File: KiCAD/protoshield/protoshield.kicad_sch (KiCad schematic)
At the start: 34 parts, among them J1 Screw_Terminal_01x03, J16 Screw_Terminal_01x05, J2 Screw_Terminal_01x02, J3 Screw_Terminal_01x02, J4 Screw_Terminal_01x02, J5 Screw_Terminal_01x02, J6 Screw_Terminal_01x03, J7 Screw_Terminal_01x03, J8 Screw_Terminal_01x03, U2 Metro_ESP32S3

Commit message: revD: Metro symbol gains SDA/SCL + protoshield wiring + analog update
xmitter.kicad_sym Metro_ESP32S3 symbol: add SDA and SCL pins
(bidirectional) at (15.24, +16.51) and (15.24, +19.05); expand body
top from +17.145 to +21.59; move Reference label to +22.86. No other
pins moved.

Protoshield schematic: wire the new Metro SDA/SCL pins through the
shield's screw-terminal boundary to the analog board I2C LV-side
entry.

Analog arduino.kicad_sch: companion updates picked up during the
I2C routing work.

Co-Authored-By: Claude Opus 4.7 <noreply@anthropic.com>
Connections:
- net SCL_IN: now also U2.SCL
- net SDA_IN: now also U2.SDA
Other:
- note added: "SCL_IN and SDA_IN go to SCL and SDA"
- note removed: "SCL_IN and SDA_IN go to SCL and SDA on Metro (not shown in symbol)"
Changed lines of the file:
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@@
 	(generator_version "10.0")
 	(paper "A4")
-	(text "SCL_IN and SDA_IN go to SCL and SDA\non Metro (not shown in symbol)"
+	(text "SCL_IN and SDA_IN go to SCL and SDA"
 		(exclude_from_sim no)
 		(at 118.618 143.764 0)
@@
 	)
 	(global_label "SCL_IN"
-		(shape output)
+		(shape bidirectional)
 		(at 107.95 142.24 0)
 		(fields_autoplaced yes)
@@
 		)
 		(property "Intersheetrefs" "${INTERSHEET_REFS}"
-			(at 117.3457 142.24 0)
+			(at 118.457 142.24 0)
 			(hide yes)
 			(show_name no)
@@
 		)
 	)
+	(global_label "SCL_IN"
+		(shape bidirectional)
+		(at 181.61 64.77 0)
+		(fields_autoplaced yes)
+		(effects
+			(font
+				(size 1.27 1.27)
+			)
+			(justify left)
+		)
+		(property "Intersheetrefs" "${INTERSHEET_REFS}"
+			(at 192.117 64.77 0)
+			(hide yes)
+			(show_name no)
+			(do_not_autoplace no)
+			(effects
+				(font
+					(size 1.27 1.27)
+				)
+				(justify left)
+			)
+		)
+	)
 	(global_label "FAULT_N_CLEAN"
 		(shape input)
@@
 	)
 	(global_label "SDA_IN"
-		(shape output)
+		(shape bidirectional)
 		(at 107.95 144.78 0)
 		(fields_autoplaced yes)
@@
 		)
 		(property "Intersheetrefs" "${INTERSHEET_REFS}"
-			(at 117.4062 144.78 0)
+			(at 118.5175 144.78 0)
 			(hide yes)
 			(show_name no)
@@
 		)
 	)
+	(global_label "SDA_IN"
+		(shape bidirectional)
+		(at 181.61 67.31 0)
+		(fields_autoplaced yes)
+		(effects
+			(font
+				(size 1.27 1.27)
+			)
+			(justify left)
+		)
+		(property "Intersheetrefs" "${INTERSHEET_REFS}"
+			(at 192.1775 67.31 0)
+			(hide yes)
+			(show_name no)
+			(do_not_autoplace no)
+			(effects
+				(font
+					(size 1.27 1.27)
+				)
+				(justify left)
+			)
+		)
+	)
 	(global_label "Source_Sense_B"
 		(shape input)
@@
 		(pin "RESET"
 		)
+		(pin "SCL"
+		)
+		(pin "SDA"
+		)
 		(instances

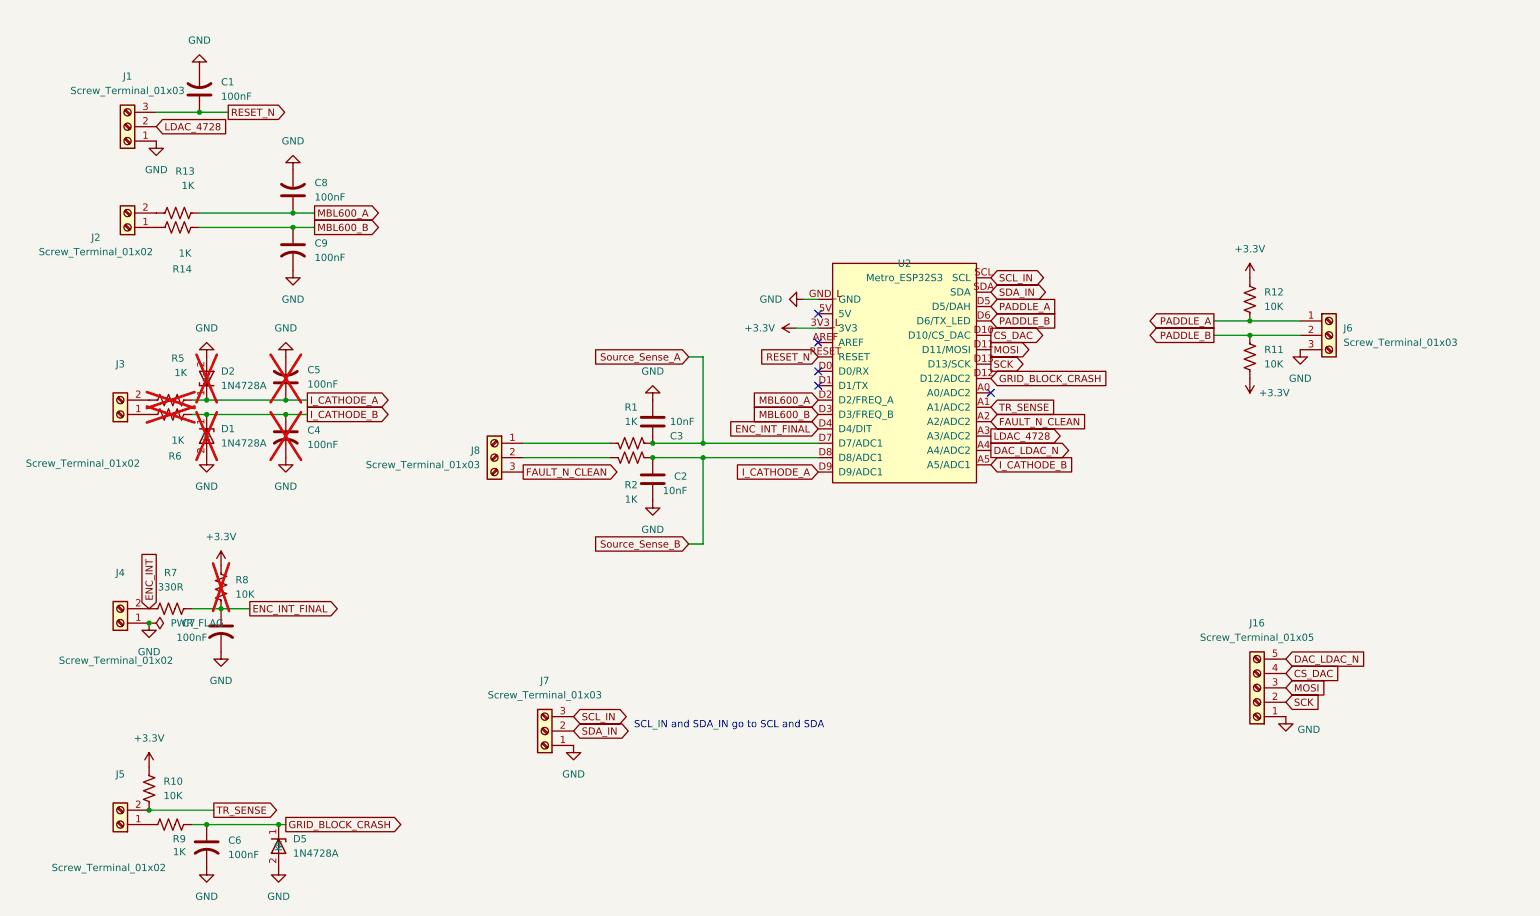
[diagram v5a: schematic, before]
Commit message: revD: Documentation handoff snapshot + protoshield/analog touch-ups
New Documentation/revD_fix_status_2026-10-24.md: handoff doc capturing
the 2026-10-22 to 10-24 claude.ai review session state -- decisions
made, schematic changes landed, items still open, with cross-refs to
the Rev D Fix Implementation Plan item IDs (A1, P2, F3, ... M/S/N).

Documentation/Components/cd54hc4049.pdf: TI CD54/74HC4049 and HC4050
datasheet archived locally.

Analog + protoshield minor schematic touches picked up during
reconciliation; netlists regenerated to match.

Co-Authored-By: Claude Opus 4.7 <noreply@anthropic.com>
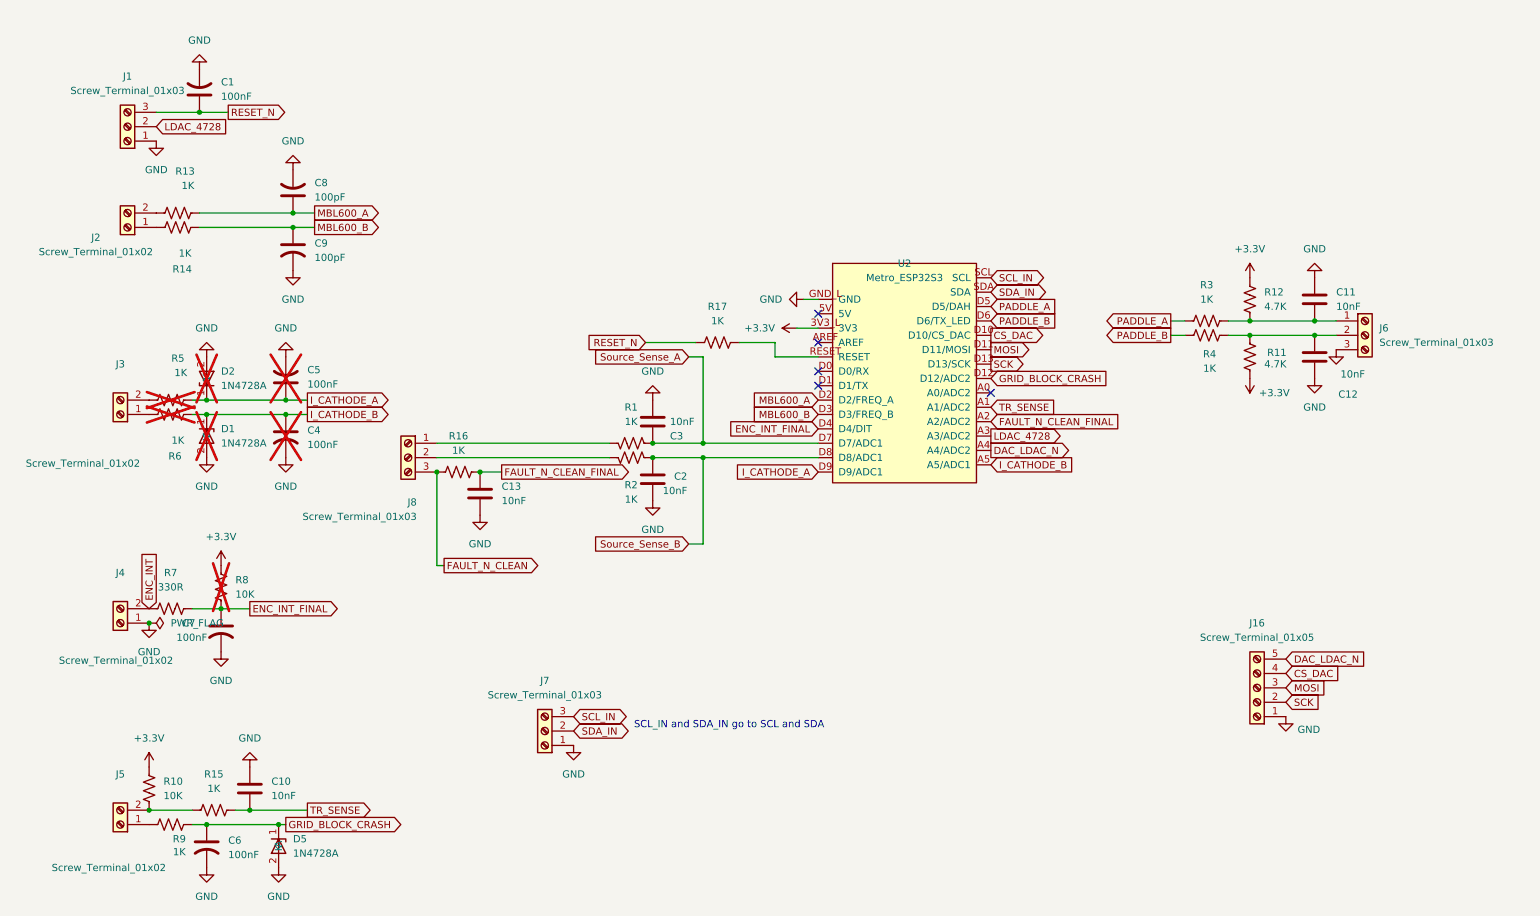
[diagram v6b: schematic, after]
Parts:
- added C10, C11, C12, C13: 10nF, symbol Device:C
- added R15, R16, R17, R3, R4: 1K, symbol Device:R_US
- C8, C9: value 100nF -> 100pF
- R11, R12: value 10K -> 4.7K
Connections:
- net FAULT_N_CLEAN: now also R16.1; no longer U2.A2 (A2/ADC2)
- net GND: now also C10.1, C11.1, C12.1, C13.2
- net PADDLE_A: now also R3.1; no longer J6.1 (Pin_1), R12.2
- net PADDLE_B: now also R4.1; no longer J6.2 (Pin_2), R11.1
- net RESET_N: now also R17.1; no longer U2.RESET
- net TR_SENSE: now also C10.2, R15.2; no longer J5.2 (Pin_2), R10.2
- new net: C11.2, J6.1 (Pin_1), R12.2, R3.2
- new net: C12.2, J6.2 (Pin_2), R11.1, R4.2
- new net: J5.2 (Pin_2), R10.2, R15.1
- new net: R17.2, U2.RESET
- new net FAULT_N_CLEAN_FINAL: C13.1, R16.2, U2.A2 (A2/ADC2)
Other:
- moved on the sheet: J6, J8

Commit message: revD: footprint pass across all boards + ss_pa fault-chain fix + LLM review brief
- New tools/assign_misc_footprints.py: lib_id-keyed footprint assigner
  (resistors, screw terminals, pin headers, LT1054); mirrors cap-script
  safe-write (UTF-8 no BOM, no CRLF translation).
- tools/assign_cap_footprints.py: added 0.47uF -> C_Rect_L7.0mm case.
- Ran both scripts across analog, ss_pa, Output LPF, frontpanel,
  protoshield, and shelved power board. ~100 fills; details in diffs.
- ss_pa: R1-R4 (0.22 ohm source sense) upgraded to 2W Yageo RSF200
  with DIN0516 L15.5mm/P20.32mm footprint; Value tagged "0.22R 2W".
  R15/R16 confirmed 1/4W (DIN0207) for BS170 source degeneration.
- analog/power: R44 15R 5W horizontal, P30.48mm footprint.
- ss_pa fault chain (from external LLM review): R21/R22 raised
  10K -> 100K to restore self-latching loop gain; new R26 = 100K
  across C12 so cap discharges between power cycles (reliable reset).
  R26 footprint pending.
- Documentation/revD_llm_review_brief.md: new, comprehensive system
  description for external LLM deep-dive (function, component values,
  power dissipation, design flaws). References all five board netlists.

Co-Authored-By: Claude Opus 4.7 <noreply@anthropic.com>
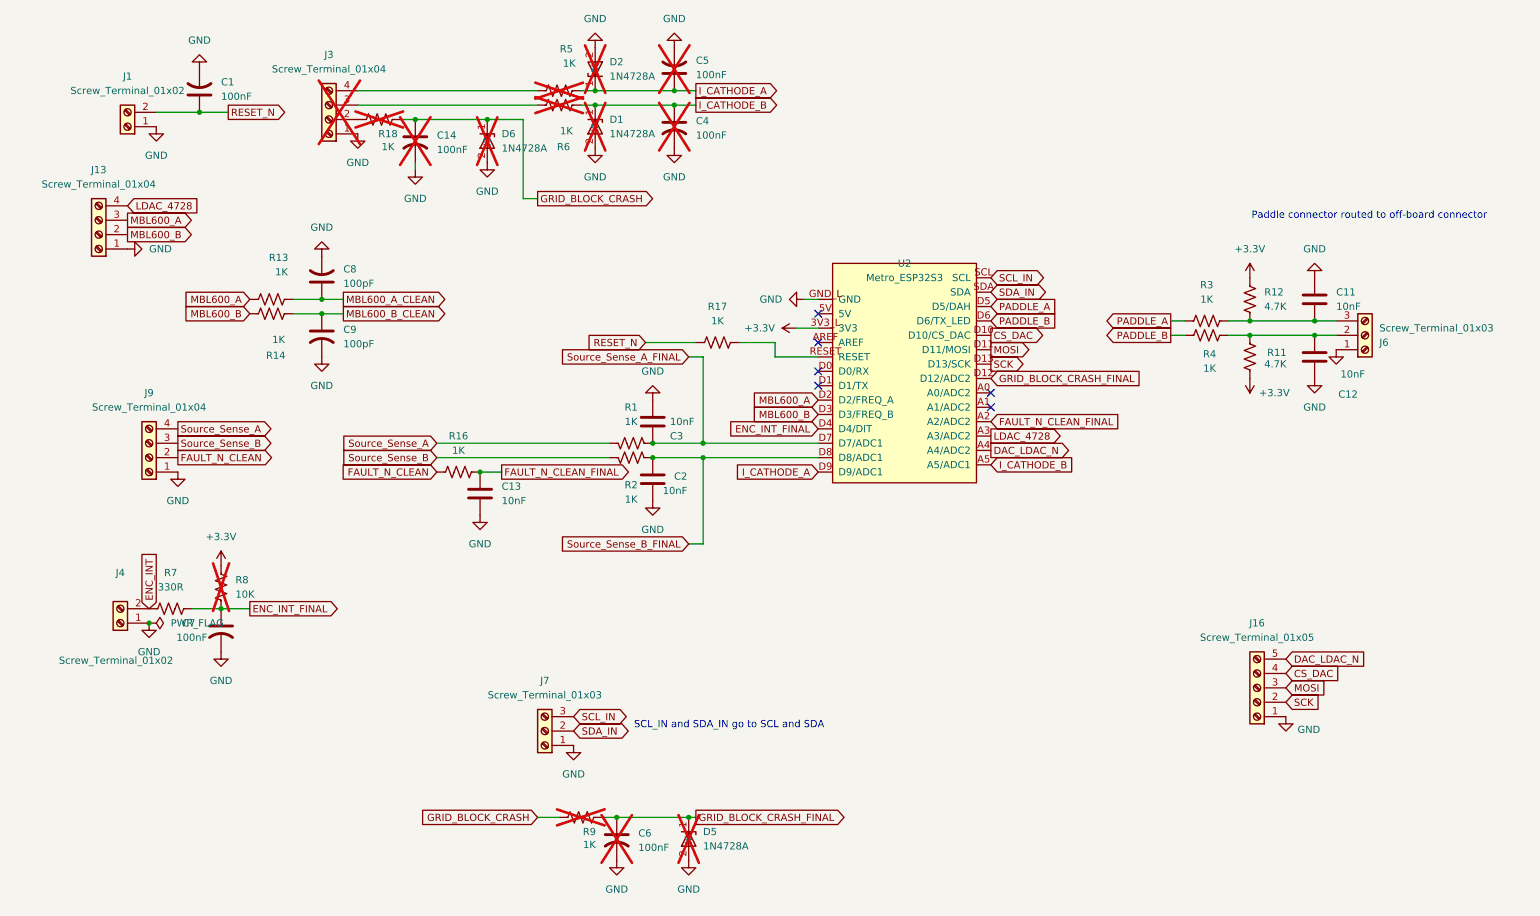
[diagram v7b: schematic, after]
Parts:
- removed C10: 10nF, symbol Device:C
- removed J1, J8: Screw_Terminal_01x03, TerminalBlock_Phoenix:TerminalBlock_Phoenix_MKDS-1,5-3_1x03_P5.00mm_Horizontal, symbol Connector:Screw_Terminal_01x03
- removed J2, J3, J5: Screw_Terminal_01x02, TerminalBlock_Phoenix:TerminalBlock_Phoenix_MKDS-1,5-2_1x02_P5.00mm_Horizontal, symbol Connector:Screw_Terminal_01x02
- removed R10: 10K, Resistor_THT:R_Axial_DIN0207_L6.3mm_D2.5mm_P10.16mm_Horizontal, symbol Device:R_US
- removed R15: 1K, symbol Device:R_US
- added C14: 100nF, Capacitor_THT:C_Disc_D5.0mm_W2.5mm_P2.50mm, symbol Device:C_US
- added D6: 1N4728A, Diode_THT:D_DO-41_SOD81_P10.16mm_Horizontal, symbol xmitter:1N4728A
- added J1: Screw_Terminal_01x02, TerminalBlock_Phoenix:TerminalBlock_Phoenix_MKDS-1,5-2_1x02_P5.00mm_Horizontal, symbol Connector:Screw_Terminal_01x02
- added J13, J3, J9: Screw_Terminal_01x04, TerminalBlock_Phoenix:TerminalBlock_Phoenix_MKDS-1,5-4_1x04_P5.00mm_Horizontal, symbol Connector:Screw_Terminal_01x04
- added R18: 1K, Resistor_THT:R_Axial_DIN0207_L6.3mm_D2.5mm_P10.16mm_Horizontal, symbol Device:R_US
- C11, C12, C13: footprint (none) -> Capacitor_THT:C_Disc_D6.0mm_W2.5mm_P5.00mm
- C6, D5, R9: now not fitted
- R16, R17, R3, R4: footprint (none) -> Resistor_THT:R_Axial_DIN0207_L6.3mm_D2.5mm_P10.16mm_Horizontal
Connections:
- net FAULT_N_CLEAN: now also J9.2 (Pin_2)
- net GND: now also J6.1 (Pin_1), C14.2, D6.2 (A), J1.1 (Pin_1), J13.1 (Pin_1), J3.1 (Pin_1), J9.1 (Pin_1); no longer J6.3 (Pin_3)
- net GRID_BLOCK_CRASH: now also R9.1, C14.1, D6.1 (K), R18.2; no longer C6.1, D5.1 (K), R9.2, U2.D12 (D12/ADC2)
- net LDAC_4728: now also J13.4 (Pin_4)
- net MBL600_A: now also R13.1, J13.3 (Pin_3); no longer C8.1, R13.2
- net MBL600_B: now also R14.1, J13.2 (Pin_2); no longer C9.1, R14.2
- net RESET_N: now also J1.2 (Pin_2)
- net Source_Sense_A: now also R1.2, J9.4 (Pin_4); no longer C3.1, R1.1, U2.D7 (D7/ADC1)
- net Source_Sense_B: now also R2.2, J9.3 (Pin_3); no longer C2.1, R2.1, U2.D8 (D8/ADC1)
- net at C11.2, R12.2, R3.2: now also J6.3 (Pin_3); no longer J6.1 (Pin_1)
- net at R6.1: now also J3.3 (Pin_3)
- net at R5.1: now also J3.4 (Pin_4)
- net TR_SENSE: no longer names the net of U2.A1 (A1/ADC2)
- new net: J3.2 (Pin_2), R18.1
- new net GRID_BLOCK_CRASH_FINAL: C6.1, D5.1 (K), R9.2, U2.D12 (D12/ADC2)
- new net MBL600_A_CLEAN: C8.1, R13.2
- new net MBL600_B_CLEAN: C9.1, R14.2
- new net Source_Sense_A_FINAL: C3.1, R1.1, U2.D7 (D7/ADC1)
- new net Source_Sense_B_FINAL: C2.1, R2.1, U2.D8 (D8/ADC1)
- no-connect marks 5 -> 6
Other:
- note added: "Paddle connector routed to off-board connector"
- moved on the sheet: C4, C5, C8, C9, D1, D2, R13, R14, R5, R6
